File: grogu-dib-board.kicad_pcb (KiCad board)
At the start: 4 copper layers, 9.5 x 102.6 mm, 18 parts, among them J1 ERF8-050-05.0-L-DV-K-TR, J2 ERF8-050-05.0-L-DV-K-TR

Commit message: final_w_updated_vias
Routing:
- net /FB2.HF4: track 6.71 -> 1.58 mm, vias 1 -> 3
- net /FB3.HF4: track 6.57 -> 1.57 mm, vias 1 -> 3
- net /FB1.HF4: track 4.94 -> 1.54 mm, vias 1 -> 3
- net /FB4.HF4: track 4.68 -> 1.60 mm, vias 1 -> 3

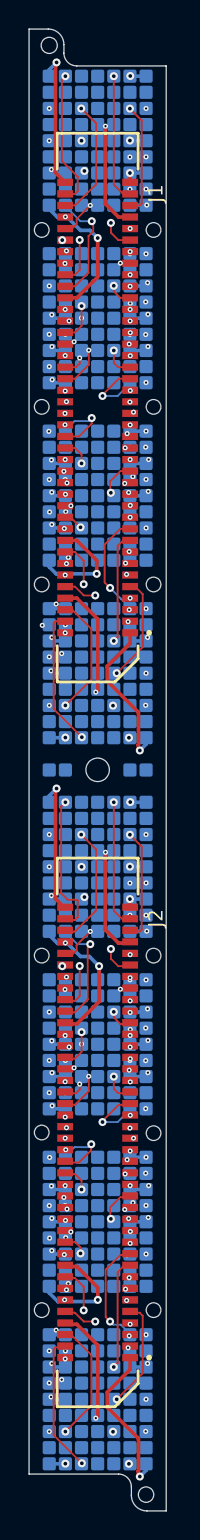
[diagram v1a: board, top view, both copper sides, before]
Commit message: fix 1-3 vias
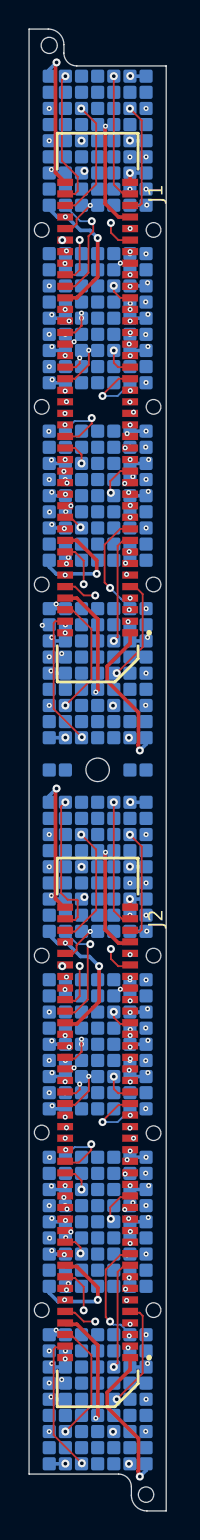
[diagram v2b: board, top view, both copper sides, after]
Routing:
- net /FB3.HS3: vias 2 -> 3
- net /FB4.HS3: vias 2 -> 3
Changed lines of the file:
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@@
 	)
 	(segment
-		(start 72.345443 58.938667)
+		(start 72.337831 60.30052)
 		(end 72.345443 60.308132)
 		(width 0.127)
@@
 		(net 4)
 	)
+	(segment
+		(start 72.337831 59.421209)
+		(end 72.337831 60.30052)
+		(width 0.127)
+		(layer "F.Cu")
+		(net 4)
+	)
+	(via micro
+		(at 72.337831 59.421209)
+		(size 0.3556)
+		(drill 0.1524)
+		(layers "F.Cu" "In1.Cu")
+		(net 4)
+	)
+	(segment
+		(start 72.345443 59.413597)
+		(end 72.337831 59.421209)
+		(width 0.127)
+		(layer "In1.Cu")
+		(net 4)
+	)
+	(segment
+		(start 72.345443 58.938667)
+		(end 72.345443 59.413597)
+		(width 0.127)
+		(layer "In1.Cu")
+		(net 4)
+	)
 	(via blind
 		(at 72.345443 58.938667)
 		(size 0.5588)
 		(drill 0.254)
-		(layers "F.Cu" "In2.Cu")
+		(layers "In1.Cu" "In2.Cu")
 		(net 4)
 	)
@@
 	)
 	(segment
-		(start 72.345443 109.230667)
-		(end 72.345443 110.600132)
+		(start 71.884875 111.0607)
+		(end 71.207875 111.0607)
 		(width 0.127)
 		(layer "F.Cu")
@@
 	)
 	(segment
-		(start 71.884875 111.0607)
-		(end 71.207875 111.0607)
+		(start 72.345443 110.600132)
+		(end 71.884875 111.0607)
 		(width 0.127)
 		(layer "F.Cu")
@@
 	)
 	(segment
-		(start 72.345443 110.600132)
-		(end 71.884875 111.0607)
+		(start 72.337831 109.713209)
+		(end 72.337831 110.59252)
 		(width 0.127)
 		(layer "F.Cu")
 		(net 346)
 	)
+	(segment
+		(start 72.337831 110.59252)
+		(end 72.345443 110.600132)
+		(width 0.127)
+		(layer "F.Cu")
+		(net 346)
+	)
+	(via micro
+		(at 72.337831 109.713209)
+		(size 0.3556)
+		(drill 0.1524)
+		(layers "F.Cu" "In1.Cu")
+		(net 346)
+	)
+	(segment
+		(start 72.345443 109.230667)
+		(end 72.345443 109.705597)
+		(width 0.127)
+		(layer "In1.Cu")
+		(net 346)
+	)
+	(segment
+		(start 72.345443 109.705597)
+		(end 72.337831 109.713209)
+		(width 0.127)
+		(layer "In1.Cu")
+		(net 346)
+	)
 	(via blind
 		(at 72.345443 109.230667)
 		(size 0.5588)
 		(drill 0.254)
-		(layers "F.Cu" "In2.Cu")
+		(layers "In1.Cu" "In2.Cu")
 		(net 346)
 	)
